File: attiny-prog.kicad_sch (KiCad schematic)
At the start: 9 parts, among them J1 SOIC16_clip

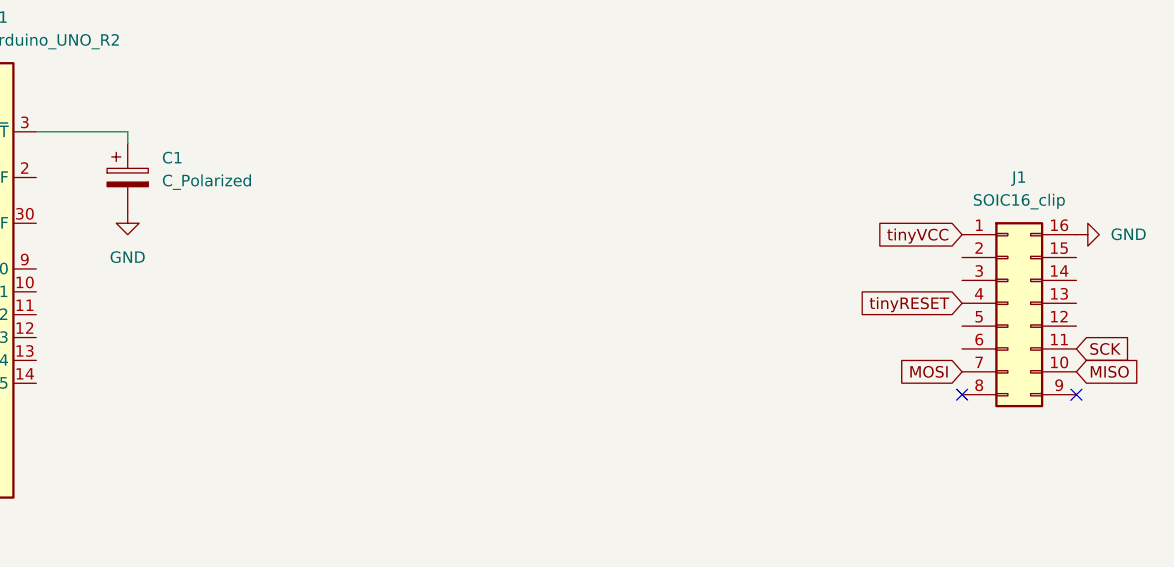
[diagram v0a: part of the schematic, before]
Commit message: Second revision
* fixed SOIC_clip header pinout
* added reset capacitor value
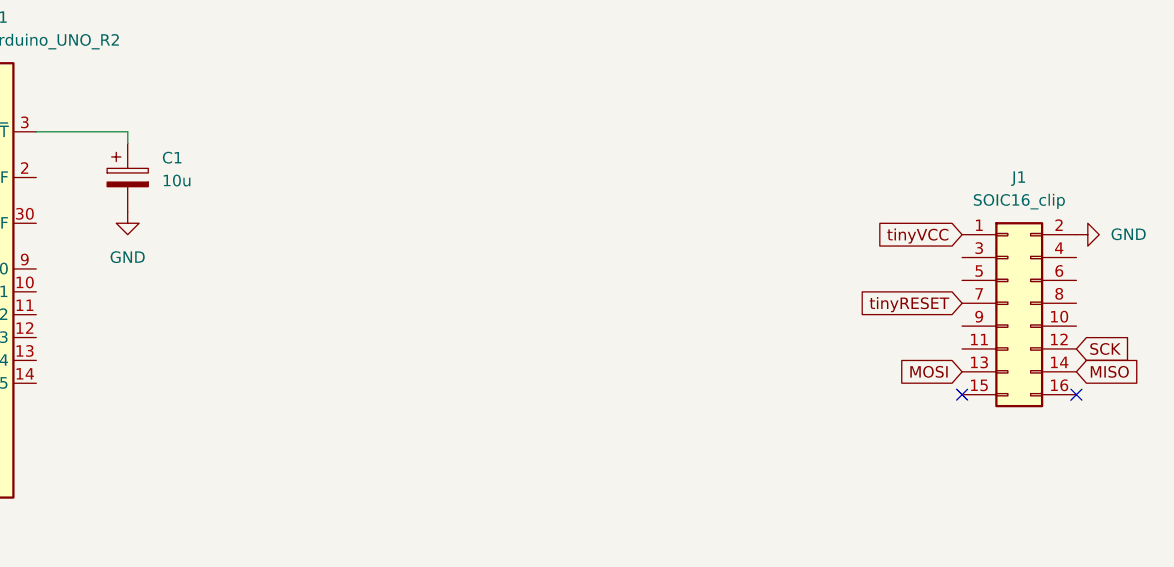
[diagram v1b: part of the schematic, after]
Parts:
- C1: value C_Polarized -> 10u
- J1: symbol Connector_Generic:Conn_02x08_Counter_Clockwise -> Connector_Generic:Conn_02x08_Odd_Even
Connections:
- net GND: now also J1.2 (Pin_2); no longer J1.16 (Pin_16)
- net MISO: now also J1.14 (Pin_14); no longer J1.10 (Pin_10)
- net MOSI: now also J1.13 (Pin_13); no longer J1.7 (Pin_7)
- net SCK: now also J1.12 (Pin_12); no longer J1.11 (Pin_11)
- net tinyRESET: now also J1.7 (Pin_7); no longer J1.4 (Pin_4)
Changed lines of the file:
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@@
 	(title_block
 		(title "ATTiny84A Programmer for Uno")
-		(date "2024-12-09")
-		(rev "rev1")
+		(date "2024-12-11")
+		(rev "rev2")
 		(company "SEM")
 		(comment 1 "ArduinoISP hat for Tiny84A & SOIC16 clip")
@@
 	)
 	(symbol
-		(lib_id "Connector_Generic:Conn_02x08_Counter_Clockwise")
+		(lib_id "Connector_Generic:Conn_02x08_Odd_Even")
 		(at 215.9 77.47 0)
 		(unit 1)
@@
 			)
 		)
-		(property "Description" "Generic connector, double row, 02x08, counter clockwise pin numbering scheme (similar to DIP package numbering), script generated (kicad-library-utils/schlib/autogen/connector/)"
+		(property "Description" "Generic connector, double row, 02x08, odd/even pin numbering scheme (row 1 odd numbers, row 2 even numbers), script generated (kicad-library-utils/schlib/autogen/connector/)"
 			(at 215.9 77.47 0)
 			(effects
@@
 			)
 		)
-		(property "Value" "C_Polarized"
+		(property "Value" "10u"
 			(at 121.92 63.8809 0)
 			(effects
